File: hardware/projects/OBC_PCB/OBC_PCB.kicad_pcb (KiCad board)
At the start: 8 copper layers, 42.2 x 67.2 mm, 136 parts, among them J1 LS021B7DD02, J2 DM3CS-SF, J3 FH12-12S-0.5SH(55), J4 1S Li-Po, J5 TC2030-CTX-NL, J7 RF coax pads, J8 RF coax pads, Q1 AO3400A, SW1 PREV, SW2 NEXT, SW3 SELECT / POWER, SW4 BACK, U1 MAX-F11N, U2 NPM1300-CAAA-R, U3 BMA400, U4 BMM350, U5 BMP581, U6 nRF54LM20A-PAAA, U7 TPS610997, Y1 32MHz, Y3 32.768kHz

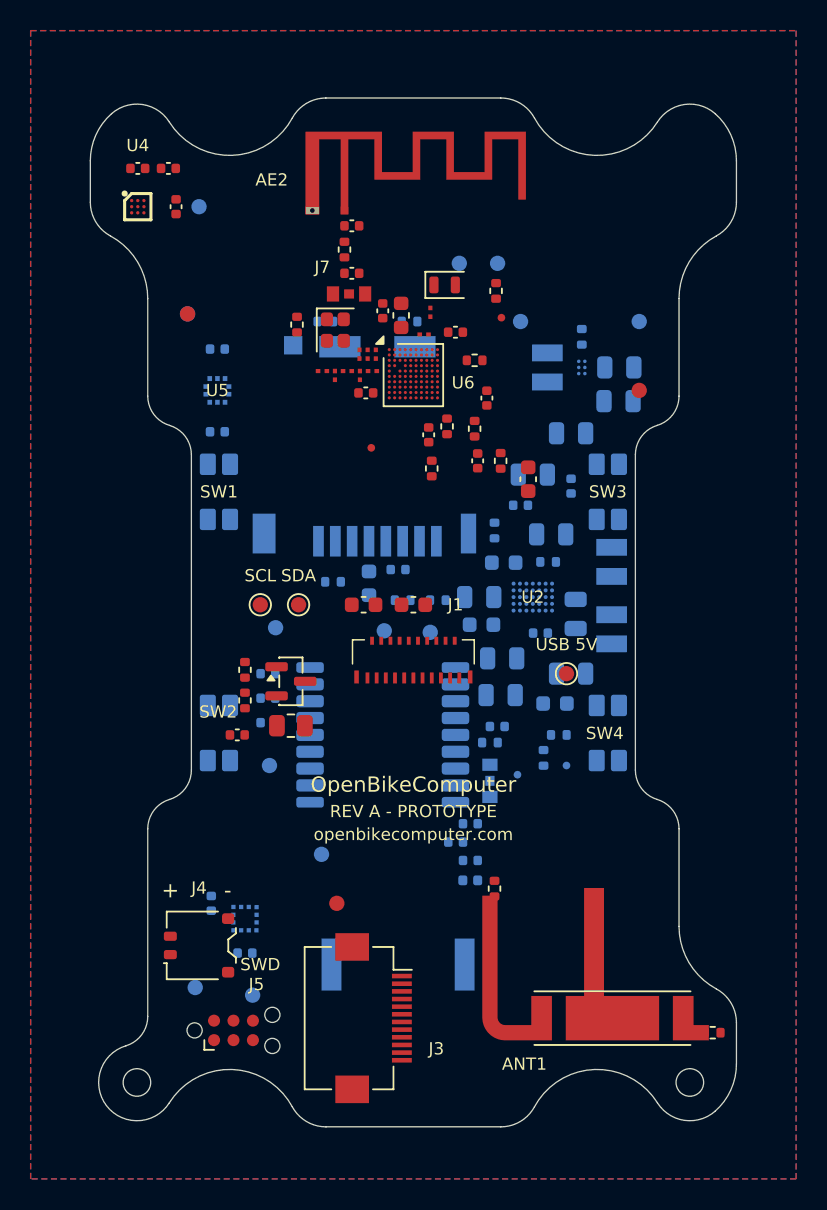
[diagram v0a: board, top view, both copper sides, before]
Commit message: hardware: route the non-HDI eight-layer PCB
Route the QFN schematic on a PCBWay standard eight-layer stack with
through vias, a 4 mil track floor and continuous reference planes.
Use horizontal, vertical and 45-degree traces on a 0.05 mm layout grid.
Add ground returns, stitch the pours and place readable service labels.

Keep the backlight connector undefined and the battery and USB connector
positions provisional. Retain fabrication and RF validation notes.
Remove duplicate schematic filter fields and duplicate power references.

Validation: native KiCad DRC/refill, schematic parity and ERC; routing
angle, ground-plane, USB and RF geometry checks. Public docs unchanged.
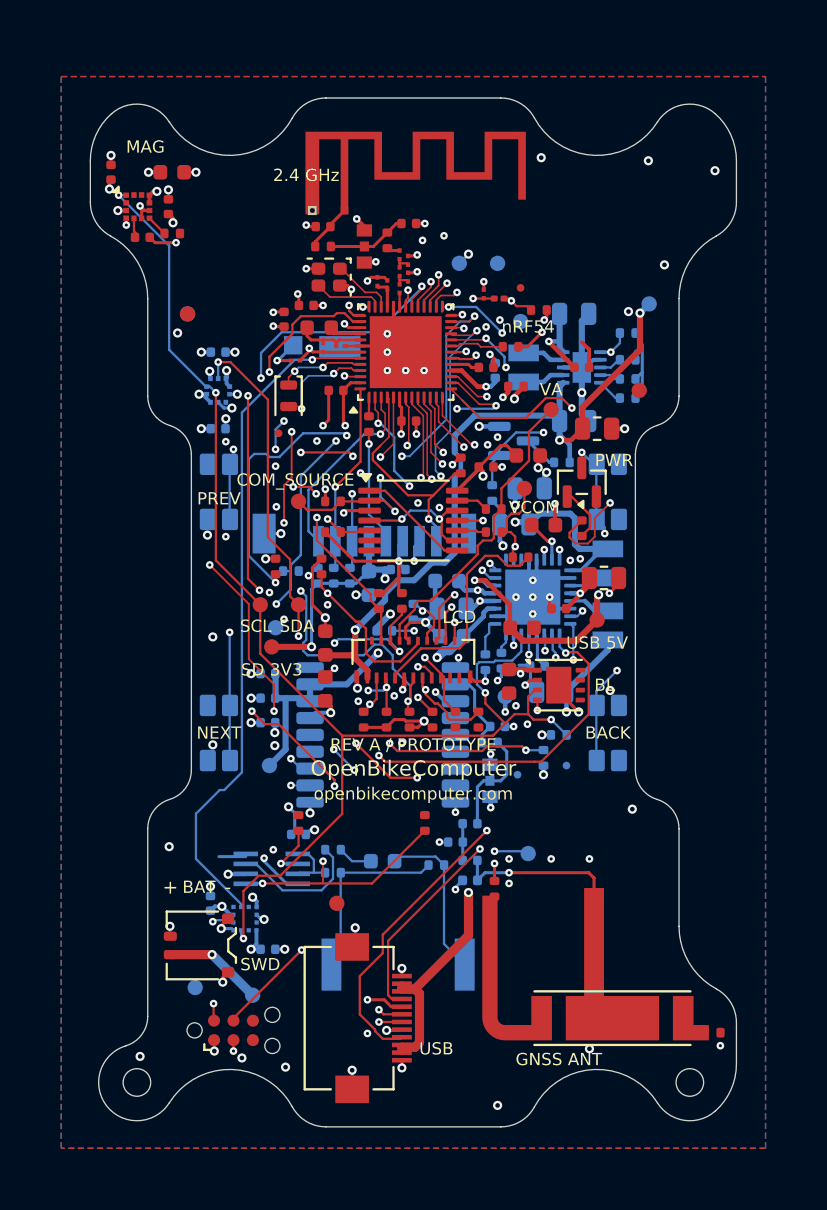
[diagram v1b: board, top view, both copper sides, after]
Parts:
- removed C18, C19: 10u, Capacitor_SMD:C_0805_2012Metric
- removed R36: 220R, Resistor_SMD:R_0805_2012Metric
- removed R37: 1k, Resistor_SMD:R_0402_1005Metric
- removed R38: 100k, Resistor_SMD:R_0402_1005Metric
- added C44: 1u, Capacitor_SMD:C_0603_1608Metric, B.Cu at (98.0, 116.2)
- added C51: 10u, Capacitor_SMD:C_0603_1608Metric, F.Cu at (84.2, 71.2)
- added C52: 100n, Capacitor_SMD:C_0402_1005Metric, B.Cu at (92.5, 114.5)
- added C53: 100n, Capacitor_SMD:C_0402_1005Metric, F.Cu at (104.8, 90.5)
- added C54: 1u, Capacitor_SMD:C_0603_1608Metric, F.Cu at (106.2, 104.5)
- added C55: 3.9p, obc:C_Nordic_0201_0603Metric, F.Cu at (104.6, 79.2)
- added D1: BAS40-7-F, Package_TO_SOT_SMD:SOT-23, F.Cu at (111.0, 91.5)
- added R34: 47k, Resistor_SMD:R_0402_1005Metric, B.Cu at (101.5, 116.5)
- added R42: 100k, Resistor_SMD:R_0402_1005Metric, F.Cu at (84.2, 75.2)
- added R43: 470R, Resistor_SMD:R_0402_1005Metric, F.Cu at (111.0, 94.5)
- added R44: 100k, Resistor_SMD:R_0402_1005Metric, F.Cu at (100.8, 113.8)
- added R45: 100k, Resistor_SMD:R_0402_1005Metric, F.Cu at (92.5, 113.8)
- added R46: 47k, Resistor_SMD:R_0402_1005Metric, F.Cu at (94.8, 92.8)
- added R47: 100k, Resistor_SMD:R_0402_1005Metric, F.Cu at (94.8, 94.8)
- added R48: 150R, Resistor_SMD:R_0402_1005Metric, F.Cu at (105.2, 94.8)
- added R49: 150R, Resistor_SMD:R_0402_1005Metric, F.Cu at (105.2, 93.2)
- added R50: 0R, Resistor_SMD:R_0402_1005Metric, F.Cu at (107.0, 96.4)
- added R51: 100k, Resistor_SMD:R_0402_1005Metric, F.Cu at (104.2, 107.0)
- added R52: 100k, Resistor_SMD:R_0402_1005Metric, B.Cu at (100.0, 100.0)
- added R53: 100k, Resistor_SMD:R_0402_1005Metric, F.Cu at (101.2, 107.0)
- added R54: 100k, Resistor_SMD:R_0402_1005Metric, F.Cu at (91.0, 97.0)
- added R55: 100k, Resistor_SMD:R_0402_1005Metric, F.Cu at (102.8, 107.0)
- added R56: 100k, Resistor_SMD:R_0402_1005Metric, B.Cu at (92.0, 97.3)
- added R57: 100k, Resistor_SMD:R_0402_1005Metric, F.Cu at (96.8, 107.0)
- added R58: 100k, Resistor_SMD:R_0402_1005Metric, F.Cu at (98.2, 107.0)
- added R59: 100k, Resistor_SMD:R_0402_1005Metric, F.Cu at (97.8, 99.2)
- added R60: 100k, Resistor_SMD:R_0402_1005Metric, F.Cu at (99.2, 99.2)
- added R61: 100k, Resistor_SMD:R_0402_1005Metric, F.Cu at (99.8, 107.0)
- added R62: 100k, Resistor_SMD:R_0402_1005Metric, F.Cu at (94.0, 97.0)
- added R63: 36.5k, Resistor_SMD:R_0402_1005Metric, B.Cu at (114.0, 83.5)
- added R64: 10.5k, Resistor_SMD:R_0402_1005Metric, B.Cu at (114.0, 84.8)
- added R65: 36.5k, Resistor_SMD:R_0402_1005Metric, B.Cu at (114.0, 86.0)
- added R66: 1k, Resistor_SMD:R_0402_1005Metric, B.Cu at (109.7, 90.2)
- added R67: 100k, Resistor_SMD:R_0402_1005Metric, B.Cu at (105.2, 92.2)
- added R68: 1k, Resistor_SMD:R_0201_0603Metric, F.Cu at (105.6, 79.5)
- added TP14: VCOM, TestPoint:TestPoint_Pad_D1.0mm, F.Cu at (107.2, 91.9)
- added TP15: VA, TestPoint:TestPoint_Pad_D1.0mm, F.Cu at (109.0, 86.8)
- added U10: SN74LVC2G00DCTR, Package_SO:SSOP-8_2.95x2.8mm_P0.65mm, B.Cu at (90.8, 116.8)
- added U8: SN74LVC02APWR, Package_SO:TSSOP-14_4.4x5mm_P0.65mm, F.Cu at (100.0, 94.0)
- added U9: LP5810BDSDR, obc:LP5810_DSD0008B, F.Cu at (109.5, 104.8)
- C10: value 10u -> 22u
- C16, C17, C20, C3, R30, TP8: moved to F.Cu
- C26, Q1, R33, R41: moved to B.Cu
- C42: value 2.2u -> 220n
- C47, C48, C50: value DNP -> tune (C0G)
- C49: value 1u -> 2.2u; footprint Capacitor_SMD:C_0402_1005Metric -> Capacitor_SMD:C_0603_1608Metric
- C9: value 10u -> 22u; moved to F.Cu
- TP9: value +1V8_MAG -> COM_SOURCE; moved to F.Cu
- U2: value NPM1300-CAAA-R -> nPM1300-QEAA; footprint obc:BGA35N44X41P5X7_237X307X51 -> Package_DFN_QFN:QFN-32-1EP_5x5mm_P0.5mm_EP3.6x3.6mm
- U4: value BMM350 -> LIS2MDL; footprint obc:BGA9_BMM350 -> Package_LGA:LGA-12_2x2mm_P0.5mm
- U6: value nRF54LM20A-PAAA -> nRF54LM20A-QGAA; footprint obc:Nordic_FCCSP-98_3.67x3.85mm_Layout10x10_P0.35mm_Offcenter -> Package_DFN_QFN:VQFN-52-1EP_6x6mm_P0.4mm_EP4.7x4.7mm
- U7: value TPS610997 -> TPS63900DSKR; footprint obc:TI_YFF0006_0.884x1.226mm_P0.4mm -> Package_SON:WSON-10-1EP_2.5x2.5mm_P0.5mm_EP1.2x2mm
- moved R33 30.4 mm to (94.8, 117.0), turned to 0 degrees
- moved R41 28.6 mm to (94.8, 115.5), turned to 0 degrees
- moved C49 26.3 mm to (107.5, 89.8)
- moved Q1 21.4 mm to (106.5, 88.8)
- moved TP9 20.3 mm to (92.5, 92.8)
- moved R29 20.3 mm to (98.1, 101.2)
- moved R28 16.7 mm to (95.8, 97.6), turned to 90 degrees
- moved TP2 13.5 mm to (107.5, 115.8)
- moved Y3 12.5 mm to (91.8, 85.8), turned to -90 degrees
- moved C20 11.7 mm to (108.5, 94.3), turned to 0 degrees
- moved C1 10.4 mm to (106.6, 94.2)
- moved C2 10.3 mm to (109.0, 105.2)
- moved C23 9.86 mm to (95.0, 85.5), turned to 180 degrees
- moved C6 9.71 mm to (107.1, 101.0), turned to 0 degrees
- moved R30 9.59 mm to (103.1, 90.4), turned to -90 degrees
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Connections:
- net /Display/FLPR.P01 renamed /Storage/SD_CLK
- BZ1 pad 2: Net-(BZ1-~-Pad2) -> Net-(BZ1-Pad2)
- C26 pad 1: /SOC_USB_VBUS -> Net-(U6A-VBUS)
- C37 pad 1: +1V8_MAG -> +3V2
- C42 pad 1: Net-(U4-CRST) -> Net-(U4-C1)
- C49 pad 1: +5V_DISP -> +3V2
- J1 pad 11: /Display/LCD.BSP -> /LCD_BSP
- J1 pad 12: /Display/FLPR.P07 -> /LCD_BCK
- J1 pad 13: /FLPR.P00 -> /LCD_R0
- J1 pad 14: /FLPR.P04 -> /LCD_R1
- J1 pad 15: /Display/FLPR.P06 -> /LCD_G0
- J1 pad 16: /Display/FLPR.P08 -> /LCD_G1
- J1 pad 17: /Display/FLPR.P09 -> /LCD_B0
- J1 pad 18: /Display/FLPR.P10 -> /LCD_B1
- J1 pad 20: /Display/LCD.VCOM -> Net-(J1-VCOM)
- J1 pad 3: /Display/LCD.GSP -> /LCD_GSP
- J1 pad 4: /Display/LCD.GCK -> /LCD_GCK
- J1 pad 5: /Display/LCD.GEN -> /LCD_GEN
- J1 pad 6: /Display/LCD.INTB -> /LCD_INTB
- J1 pad 7: /Display/LCD.VB -> Net-(J1-VB)
- J1 pad 8: /Display/LCD.VA -> Net-(J1-VA)
- J2 pad 1: /Display/FLPR.P03 -> /SD_D2
- J2 pad 2: /FLPR.P00 -> /SD_D3
- J2 pad 3: /Display/FLPR.P05 -> /SD_CMD
- J2 pad 7: /Display/FLPR.P02 -> /SD_D0
- J2 pad 8: /FLPR.P04 -> /SD_D1
- J3 pad 4: /Power Management/USB_CC1 -> Net-(J3-CC1)
- J3 pad 6: /Power Management/USB_D+ -> /USB_D+
- J3 pad 7: /Power Management/USB_D- -> /USB_D-
- J3 pad 9: /Power Management/USB_CC2 -> Net-(J3-CC2)
- L1 pad 2: /Power Management/PMIC_SW1 -> Net-(U2-SW1)
- L2 pad 2: /Power Management/PMIC_SW2 -> Net-(U2-SW2)
- L3 pad 1: /SOC_DCC -> Net-(U6A-DCC)
- L5 pad 1: VSYS -> Net-(U7-LX1)
- L5 pad 2: /Power Management/BOOST_SW -> Net-(U7-LX2)
- L6 pad 1: Net-(U6A-DECRF) -> Net-(U6A-DECA)
- L6 pad 2: Net-(U6A-DECA) -> Net-(U6A-DECRF)
- Q1 pad 1: Net-(Q1-G) -> /Power Management/DISP_DISCHARGE
- Q1 pad 3: /Display/BL_K -> Net-(Q1-D)
- R23 pad 2: /SDA -> /SCL
- R24 pad 2: /SCL -> /SDA
- R28 pad 2: /Display/FLPR.P05 -> /SD_CMD
- R29 pad 2: /Display/FLPR.P02 -> /SD_D0
- R3 pad 1: /DISP_5V_EN -> /Power Management/DISP_5V_EN
- R30 pad 2: /FLPR.P04 -> /SD_D1
- R31 pad 2: /Display/FLPR.P03 -> /SD_D2
- R32 pad 2: /FLPR.P00 -> /SD_D3
- R33 pad 1: /PIEZO_A -> Net-(R33-Pad1)
- R41 pad 1: /PIEZO_B -> Net-(R41-Pad1)
- R41 pad 2: Net-(BZ1-~-Pad2) -> Net-(C44-Pad1)
- R5 pad 2: /SOC_USB_VBUS -> Net-(U6A-VBUS)
- R9 pad 1: Net-(U6D-P2.01) -> /SD_CLK_RAW
- TP9 pad 1: +1V8_MAG -> /COM_SOURCE
- U5 pad 7: /BARO_INT -> GND
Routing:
- net GND: track 0.00 -> 136.5 mm, vias 0 -> 115
- net /SDA: track 0.00 -> 116.5 mm, vias 0 -> 10
- net /SCL: track 0.00 -> 113.3 mm, vias 0 -> 7
- net /BUZZER_PWM: track 0.00 -> 82.3 mm, vias 0 -> 8
- net /nRESET: track 0.00 -> 69.7 mm, vias 0 -> 3
- net /PMIC_INT: track 0.00 -> 65.0 mm, vias 0 -> 5
- net /SWDCLK: track 0.00 -> 62.4 mm, vias 0 -> 4
- net /SWDIO: track 0.00 -> 59.5 mm, vias 0 -> 3
- net /LCD_B1: track 0.00 -> 57.0 mm, vias 0 -> 6
- net /Power Management/SHPHLD: track 0.00 -> 54.7 mm, vias 0 -> 6
- net /LCD_G1: track 0.00 -> 54.6 mm, vias 0 -> 6
- net +3V2: track 0.00 -> 54.1 mm, vias 0 -> 33
- net /COM_EN: track 0.00 -> 52.1 mm, vias 0 -> 5
- net /USB_D-: track 0.00 -> 51.6 mm, vias 0 -> 2
- net /USB_D+: track 0.00 -> 51.5 mm, vias 0 -> 2
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- added copper zone on In2.Cu, net GND
- added copper zone on In5.Cu, net GND
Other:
- rule pad_to_mask_clearance: 0 -> 0.0508
- board text added: "2.4 GHz"
- board text added: "5V"
- board text added: "ACCEL"
- board text added: "ASSEMBLY: Keep supplied exposed-pad paste windows; no paste over thermal drills. Thermal vias are ordinary unfilled, uncapped through holes. Tent the opposite side. Confirm stencil thickness and acceptable solder voiding with the assembler."
- board text added: "BACK"
- board text added: "BACKLIGHT: U9 driver fitted. J6 connector and LED load remain undefined."
- board text added: "BARO"
- board text added: "BAT"
- board text added: "BL"
- board text added: "COM_SOURCE"
- board text added: "GNSS"
- board text added: "GNSS ANT"
- board text added: "GNSS REVIEW: BSP, GEN and SHPHLD retain short B.Cu paths under U1. Preserve L7 ground. Qualify GNSS with display refresh, buzzer PWM and power-state changes in the final enclosure."
- board text added: "LAYOUT GRID: 0.05 mm. Preserve mechanical datums and footprint pad centers."
- board text added: "LCD"
- board text added: "LOCAL MASK: U6/U5/U7/J3 expansion 0.045 mm; confirm with PCBWay. GANGED MASK: U4/R68 only. Paste apertures remain separate. All other footprints retain the 0.102 mm minimum mask web."
- board text added: "MAG"
- board text added: "NEXT"
- board text added: "PCBWay regular #1: 2116 0.1195 / core 0.230 / 7628 0.175 / core 0.230 mm; symmetric. Minimum trace 0.102 mm (4 mil); clearance 0.127 mm (5 mil). No blind or laser vias. Confirm pressed dielectric and 50-ohm RF / 90-ohm USB geometry with the fabricator."
- board text added: "PCBWay regular 8-layer #1 / 1.6 mm nominal / 1 oz finished copper / ENIG. Use 0.5 oz outer starting foil plated to 1 oz."
- board text added: "PMIC"
- board text added: "PREV"
- board text added: "PWR"
- board text added: "Prototype: verify QFN RF reference, impedance, antenna tuning and mechanical fit."
- board text added: "REV A / PROTOTYPE"
- board text added: "RF"
- board text added: "Through vias only: 0.20 mm minimum drill; 0.15 mm minimum annular ring."
- board text added: "USB"
- board text added: "USB and battery connector positions remain provisional. Backlight connector pending."
- board text added: "VA"
- board text added: "VCOM"
- board text added: "microSD"
- board text added: "nRF54"
- board text removed: "1V8"
- board text removed: "BACKLIGHT: Q1/R36-R38/C49 placed; J6 connector/tail footprint TBD."
- board text removed: "BMM350: Bosch guide 3.9 says no ENIG. Confirm compatible PCB finish before fabrication."
- board text removed: "PCBWay HDI / 8 layers / 1.6mm target. Confirm stackup and 0.35mm CSP escape."
- board text removed: "PROVISIONAL 3+2+3 HDI, 1.6 mm. 35/18 um Cu; 100 um build-up; 802 um core. FR4 Dk 4.2 assumed. Fab to confirm stack, impedance, finish and CSP lands. Filled/capped microvias. RF 50-ohm / USB 90-ohm geometry pending stackup."
- board text removed: "Prototype: validate stackup, CSP lands, antenna tuning and mechanical fit."
- board text removed: "REV A - PROTOTYPE"
- board text removed: "USB + BATTERY: front access below display. Backlight connector pending."

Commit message: hardware: adapt the PCB to the JLCPCB 3313 stack
Select JLC08161H-3313 with 1 oz outer and 0.5 oz inner copper. Preserve
the USB pair geometry and use 0.18 mm outer RF feeds. Update drill,
mask and silkscreen rules, and specify epoxy-filled, capped through vias.

Keep U6's fine-pitch lands pending explicit fabrication acceptance.
The layout remains a prototype with provisional connectors and RF tuning.

Validation: native KiCad DRC/refill, schematic parity, routing angles,
plane continuity and unchanged USB geometry; impedance and DC drop
estimates. Public docs unchanged.
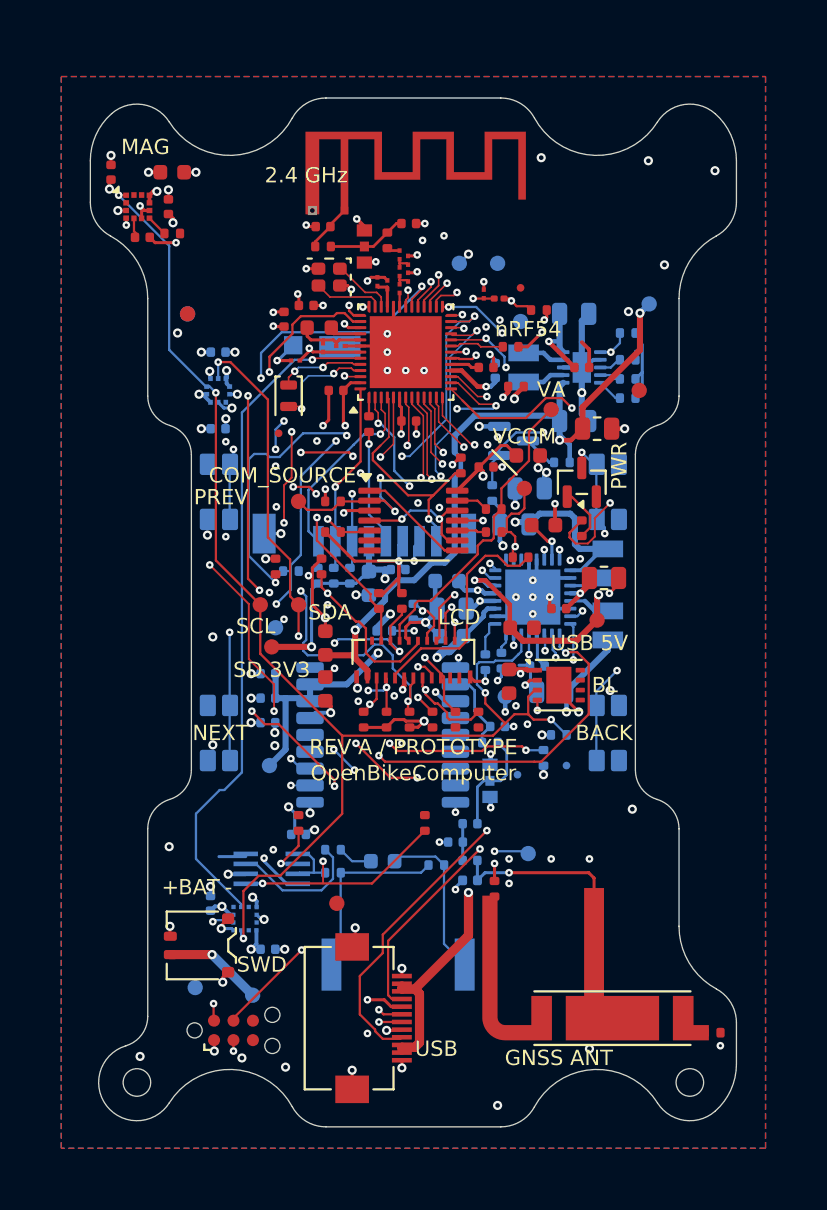
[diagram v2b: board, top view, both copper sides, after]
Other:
- board text added: "ASSEMBLY: Keep supplied exposed-pad paste windows. Confirm stencil thickness and voiding. All via holes (0.20 / 0.30 mm drill) are epoxy filled and copper capped; do not fill component holes. Select JLCPCB Epoxy Filled & Capped. Preserve the solder-mask tenting shown."
- board text added: "JLC08161H-3313 / 1.6 mm nominal / 1 oz outer, 0.5 oz inner / ENIG / green mask."
- board text added: "JLC08161H-3313: 3313 0.0994 / core 0.100 / 3x2116 0.3568 / core 0.300 mm; symmetric. Select this stack explicitly. Minimum trace 0.102 mm; clearance 0.127 mm. Through vias only. 50-ohm RF: 0.18 mm outer. 90-ohm USB: 0.125 mm width / 0.225 mm gap on L6. Confirm impedance geometry and tolerance with the fabricator."
- board text added: "LOCAL MASK: U6/U5/U7/J3 expansion 0.045 mm; C24 0.040 mm. J2 pads 9/S2/S5 expansion 0.080 mm; retain the other J2 pad openings. GANGED MASK: U4/R68 only. Paste apertures remain separate. Retain 0.102 mm minimum mask web and 0.09 mm mask-to-neighboring-copper clearance."
- board text added: "Prototype: verify LM20 QFN RF reference, impedance, antenna tuning and mechanical fit. JLCPCB file audit must accept U6 0.20 mm lands at 0.40 mm pitch before fabrication."
- board text removed: "ASSEMBLY: Keep supplied exposed-pad paste windows; no paste over thermal drills. Thermal vias are ordinary unfilled, uncapped through holes. Tent the opposite side. Confirm stencil thickness and acceptable solder voiding with the assembler."
- board text removed: "LOCAL MASK: U6/U5/U7/J3 expansion 0.045 mm; confirm with PCBWay. GANGED MASK: U4/R68 only. Paste apertures remain separate. All other footprints retain the 0.102 mm minimum mask web."
- board text removed: "PCBWay regular #1: 2116 0.1195 / core 0.230 / 7628 0.175 / core 0.230 mm; symmetric. Minimum trace 0.102 mm (4 mil); clearance 0.127 mm (5 mil). No blind or laser vias. Confirm pressed dielectric and 50-ohm RF / 90-ohm USB geometry with the fabricator."
- board text removed: "PCBWay regular 8-layer #1 / 1.6 mm nominal / 1 oz finished copper / ENIG. Use 0.5 oz outer starting foil plated to 1 oz."
- board text removed: "Prototype: verify QFN RF reference, impedance, antenna tuning and mechanical fit."
